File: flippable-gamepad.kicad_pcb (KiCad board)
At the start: 2 copper layers, 228.6 x 100 mm, 87 parts

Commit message: Fresh start
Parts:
- removed D37, D38, D39, D40, D41, D42, D43: D_Small, Diode_SMD:D_SOD-123
- removed MX37: MX-NoLED, MX_Only:MXOnly-3U-NoLED
- removed MX38, MX39, MX41, MX42, MX43: MX-NoLED, MX_Only:MXOnly-1U-NoLED
- removed MX40: MX-NoLED, MX_Only:MXOnly-1.25U-NoLED
- D1, D10, D11, D12, D13, D14, D15, D16, D17, D18, D19, D2, D20, D21, D22, D23, D24, D25, D26, D27, D28, D29, D3, D30, D31, D32, D33, D34, D35, D36, D4, D5, D6, D7, D8, D9: footprint Diode_SMD:D_SOD-123 -> Diode_THT:D_DO-35_SOD27_P7.62mm_Horizontal; moved to F.Cu
- MX1, MX16, MX24, MX32, MX8: footprint MX_Only:MXOnly-1U-NoLED -> MX_Only:MXOnly-1.25U-Reversible-NoLED
- MX10, MX11, MX12, MX13, MX14, MX15, MX18, MX19, MX2, MX20, MX21, MX22, MX23, MX25, MX26, MX28, MX29, MX3, MX30, MX31, MX33, MX36, MX4, MX5, MX6, MX9: footprint MX_Only:MXOnly-1U-NoLED -> MX_Only:MXOnly-1U-Reversible-NoLED
- MX17, MX27, MX34, MX7: footprint MX_Only:MXOnly-1.25U-NoLED -> MX_Only:MXOnly-1U-Reversible-NoLED
- MX35: footprint MX_Only:MXOnly-1U-NoLED -> MX_Only:MXOnly-3U-Reversible-ReversedStabilizers-NoLED
- moved ProMicro1 185.5 mm to (67.0, 54.9)
- moved MX36 158.9 mm to (208.0, 125.4)
- moved D36 147.2 mm to (198.4, 129.4), turned to 90 degrees
- moved MX21 139.9 mm to (188.9, 87.3)
- moved MX22 139.9 mm to (208.0, 87.3)
- moved D22 128.2 mm to (198.4, 91.3), turned to 90 degrees
- moved D21 128.2 mm to (179.4, 91.3), turned to 90 degrees
- moved MX29 120.9 mm to (188.9, 106.4)
- moved MX28 120.9 mm to (169.9, 106.4)
- moved MX30 120.9 mm to (208.0, 106.4)
- moved D8 114.6 mm to (81.8, 72.2), turned to 90 degrees
- moved D10 112.3 mm to (122.2, 72.2), turned to 90 degrees
- moved D9 112.3 mm to (103.2, 72.2), turned to 90 degrees
- moved D28 109.2 mm to (160.3, 110.3), turned to 90 degrees
- moved D30 109.2 mm to (198.4, 110.3), turned to 90 degrees
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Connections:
- D10 pad 1: ROW0 -> ROW1
- D15 pad 1: ROW1 -> ROW2
- D16 pad 1: ROW1 -> ROW2
- D17 pad 1: ROW1 -> ROW2
- D18 pad 1: ROW1 -> ROW2
- D19 pad 1: ROW1 -> ROW2
- D20 pad 1: ROW1 -> ROW2
- D23 pad 1: ROW2 -> ROW3
- D24 pad 1: ROW2 -> ROW3
- D25 pad 1: ROW2 -> ROW3
- D26 pad 1: ROW2 -> ROW3
- D27 pad 1: ROW2 -> ROW3
- D31 pad 1: ROW3 -> ROW4
- D32 pad 1: ROW3 -> ROW4
- D33 pad 1: ROW3 -> ROW4
- D34 pad 1: ROW3 -> ROW4
- D35 pad 1: ROW3 -> ROW4
- D8 pad 1: ROW0 -> ROW1
- D9 pad 1: ROW0 -> ROW1
- MX1 pad 1: COL0 -> COL1
- MX10 pad 1: COL9 -> COL3
- MX11 pad 1: COL0 -> COL4
- MX12 pad 1: COL1 -> COL5
- MX13 pad 1: COL2 -> COL6
- MX14 pad 1: COL3 -> COL7
- MX15 pad 1: COL4 -> COL0
- MX16 pad 1: COL5 -> COL1
- MX17 pad 1: COL6 -> COL2
- MX18 pad 1: COL7 -> COL3
- MX19 pad 1: COL8 -> COL4
- MX2 pad 1: COL1 -> COL2
- MX20 pad 1: COL9 -> COL5
- MX21 pad 1: COL0 -> COL6
- MX22 pad 1: COL1 -> COL7
- MX23 pad 1: COL2 -> COL0
- MX24 pad 1: COL3 -> COL1
- MX25 pad 1: COL4 -> COL2
- MX26 pad 1: COL5 -> COL3
- MX27 pad 1: COL6 -> COL4
- MX28 pad 1: COL0 -> COL5
- MX29 pad 1: COL1 -> COL6
- MX3 pad 1: COL2 -> COL3
- MX30 pad 1: COL2 -> COL7
- MX31 pad 1: COL3 -> COL0
- MX32 pad 1: COL4 -> COL1
- MX33 pad 1: COL5 -> COL2
- MX34 pad 1: COL6 -> COL3
- MX35 pad 1: COL8 -> COL5
- MX36 pad 1: COL0 -> COL7
- MX4 pad 1: COL3 -> COL4
- MX5 pad 1: COL4 -> COL5
- MX6 pad 1: COL5 -> COL6
- MX7 pad 1: COL6 -> COL7
- MX8 pad 1: COL7 -> COL1
- MX9 pad 1: COL8 -> COL2
- ProMicro1 pad 10: Net-(ProMicro1-Pad10) -> ROW2
- ProMicro1 pad 11: Net-(ProMicro1-Pad11) -> ROW1
- ProMicro1 pad 12: Net-(ProMicro1-Pad12) -> ROW0
- ProMicro1 pad 13: Net-(ProMicro1-Pad13) -> COL0
- ProMicro1 pad 14: Net-(ProMicro1-Pad14) -> COL1
- ProMicro1 pad 15: Net-(ProMicro1-Pad15) -> COL2
- ProMicro1 pad 16: Net-(ProMicro1-Pad16) -> COL3
- ProMicro1 pad 17: Net-(ProMicro1-Pad17) -> COL4
- ProMicro1 pad 18: Net-(ProMicro1-Pad18) -> COL5
- ProMicro1 pad 19: Net-(ProMicro1-Pad19) -> COL6
- ProMicro1 pad 20: Net-(ProMicro1-Pad20) -> COL7
- ProMicro1 pad 8: Net-(ProMicro1-Pad8) -> ROW4
- ProMicro1 pad 9: Net-(ProMicro1-Pad9) -> ROW3
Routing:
- net COL7: track 76.2 -> 255.8 mm
- net COL5: track 76.2 -> 213.0 mm
- net COL6: track 76.2 -> 206.9 mm
- net COL3: track 57.2 -> 182.5 mm
- net COL4: track 76.2 -> 174.0 mm
- net COL2: track 76.2 -> 164.1 mm
- net COL1: track 57.2 -> 139.9 mm
- net COL9: track 76.2 -> 0.00 mm
- net COL8: track 76.2 -> 0.00 mm
- net ROW1: track 192.0 -> 144.9 mm
- net ROW2: track 122.3 -> 168.3 mm
- net ROW0: track 189.5 -> 146.2 mm
- net ROW4: track 189.1 -> 211.5 mm
- net GND: track 0.00 -> 18.8 mm
- net ROW3: track 171.9 -> 189.6 mm
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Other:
- board size 228.6 x 100 mm -> 163.5 x 95.3 mm
- net class Default: trace_width 0.25 -> 0.254
- net class Power added: clearance 0.2, trace_width 0.381, via_dia 0.8, via_drill 0.4

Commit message: Update silkscreen
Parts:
- FACE DOWN: renamed from ProMicro1
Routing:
- net Net-(D15-Pad2): track 5.08 -> 12.7 mm
- added copper zone on F.Cu, net GND
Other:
- board size 163.5 x 95.3 mm -> 169.9 x 95.3 mm
- board text added: "C0"
- board text added: "C1"
- board text added: "C2"
- board text added: "C3"
- board text added: "C4"
- board text added: "C5"
- board text added: "C6"
- board text added: "C7"
- board text added: "Components FACE DOWN"
- board text added: "Components FACE UP"
- board text added: "GND"
- board text added: "MX35"
- board text added: "MX36"
- board text added: "R1"
- board text added: "R2"
- board text added: "R3"
- board text added: "R4"
- board text added: "RAW"
- board text added: "RIP AND TEAR, UNTIL IT'S DONE."
- board text added: "RST"
- board text added: "VCC"
- board text added: "χboard V0.1α - Designed by Kyek in Italy"

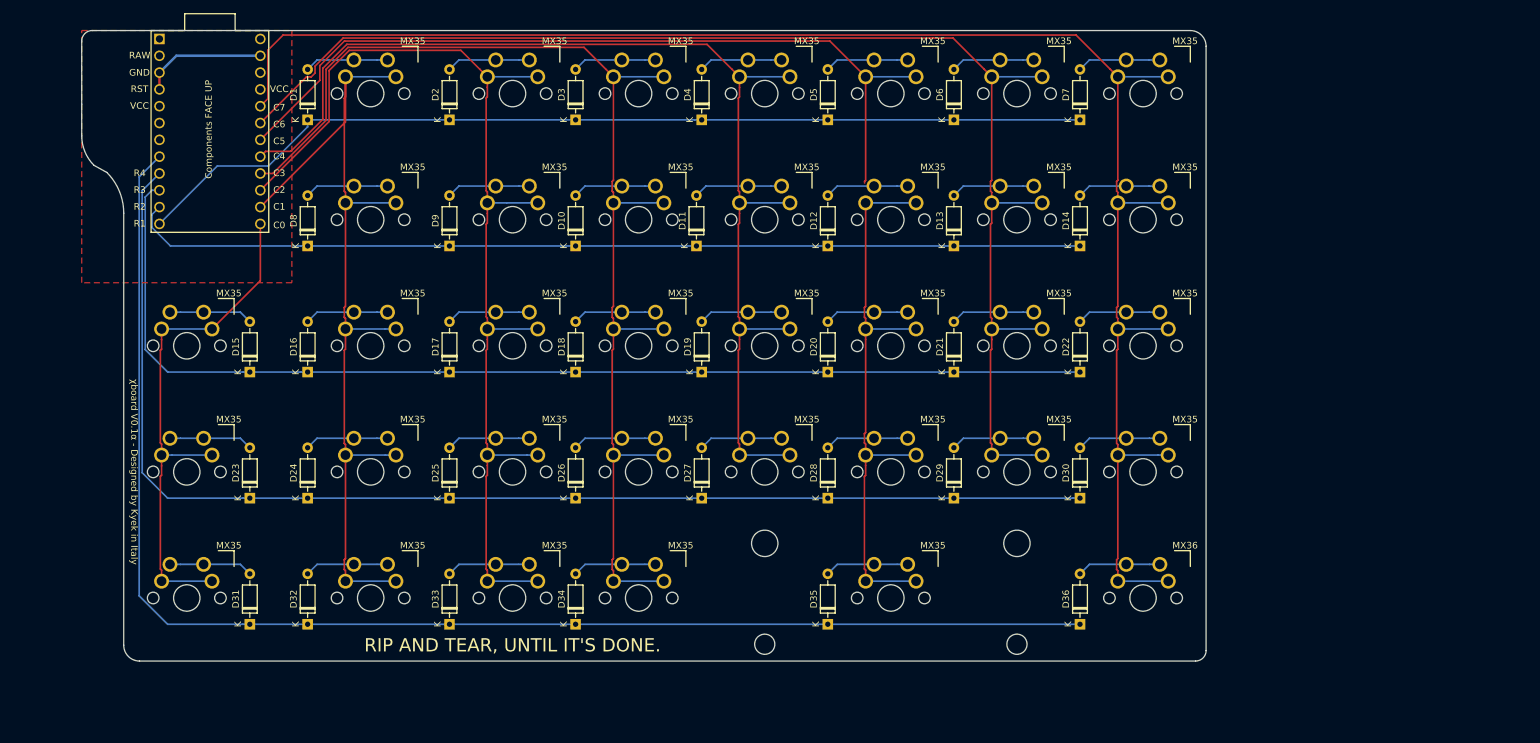
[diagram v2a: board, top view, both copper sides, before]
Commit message: Front silk screen
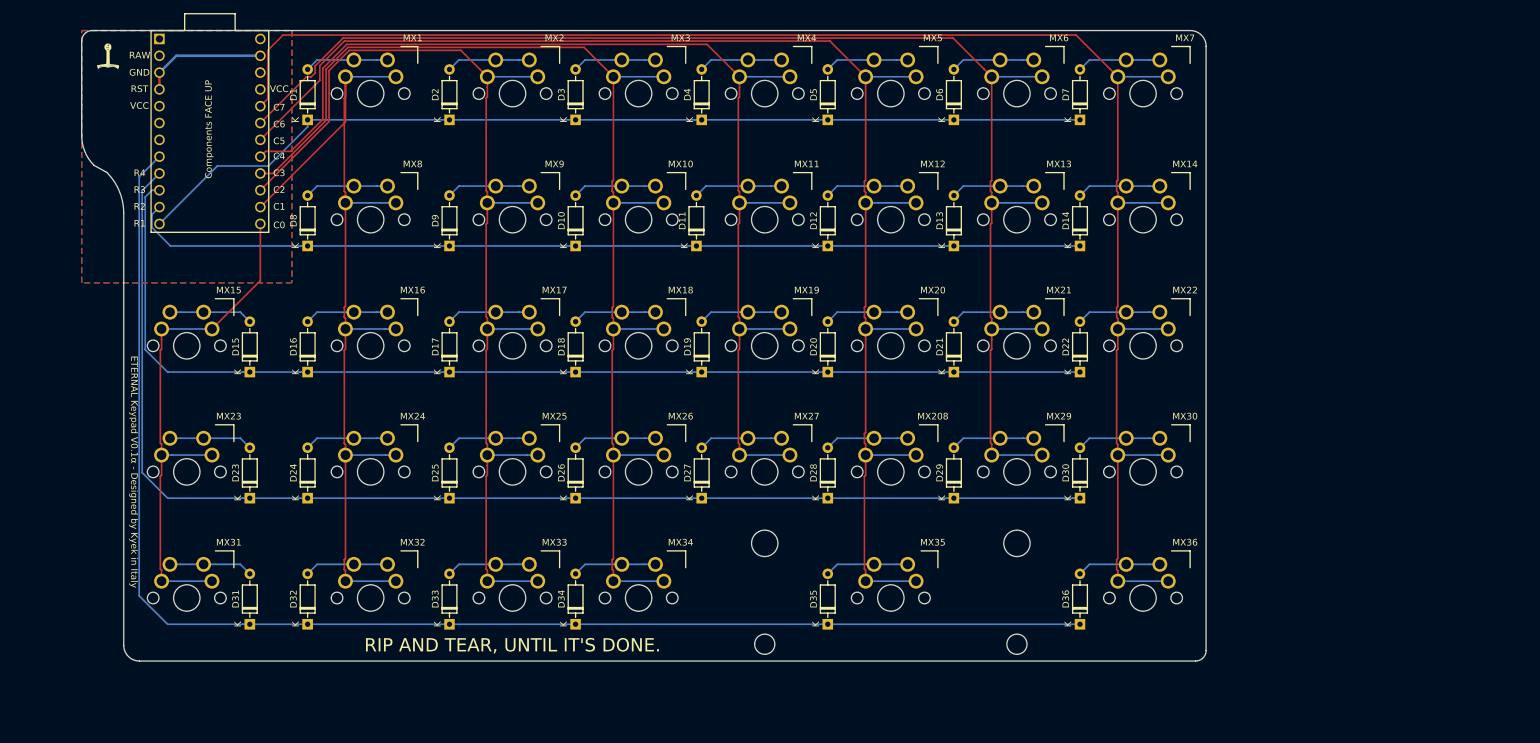
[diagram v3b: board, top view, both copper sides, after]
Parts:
- added Blade: LOGO, Symbol:excalibur-blade, B.Cu at (51.6, 49.2)
- added Blade: LOGO, Symbol:excalibur-blade, F.Cu at (51.6, 49.2)
- added Handle: LOGO, Symbol:excalibur-handle, F.Cu at (51.6, 49.2)
- added Handle: LOGO, Symbol:excalibur-handle, B.Cu at (51.6, 49.2)
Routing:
- net COL5: track 213.0 -> 216.1 mm
- added copper zone on B.Cu, net GND
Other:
- board text added: "ETERNAL Keypad V0.1α - Designed by Kyek in Italy"
- board text removed: "MX35"
- board text removed: "MX36"
- board text removed: "χboard V0.1α - Designed by Kyek in Italy"
